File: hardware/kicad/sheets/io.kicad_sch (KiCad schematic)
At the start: 22 parts, among them J10 AUX, J11 INPUTS, Q2 AO3400A, U6 ULN2003A

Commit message: hardware: uncross the AUX bank - vent on GPIO16, U6 channels reversed
U6's outputs sit level with their inputs, so channel 1 (pins 1/16, the
bottom of the SOIC) fed J10.2 at the top of the terminal and all three
output traces crossed, two of them through B.Cu. AUX1 now uses channel 3
and AUX3 channel 1, so O3/O2/O1 fan straight across to J10.2/3/4 on F.Cu
with no via (was 1/1/0 vias).

The input copper was already in the order the board's geography forces:
U6's top input escapes by the B.Cu lane north to U1 pin 9, the bottom
one by the route south of LCD_CS to U1 pin 22. Rather than re-route it,
the GPIOs follow it: vent (AUX1) moves GPIO14 -> GPIO16, AUX3 moves
GPIO16 -> GPIO14, AUX2 stays on GPIO15. The existing input tracks keep
their geometry under the swapped names, and R23/R25 trade places so each
pulldown stays on the input it terminates. U6->J10 is wired by label
pairs now, since the schematic can't draw the swap without a crossing.

Kconfig defaults, pin-assignments, the roadmap, the KiCad README and
DESIGN-NOTES follow. An existing local sdkconfig keeps the old values
until KILN_PIN_VENT / KILN_PIN_AUX3 are reset.

Co-Authored-By: Claude Opus 5.5 <noreply@anthropic.com>
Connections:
- net AUX1: now also U6.3 (I3); no longer U6.1 (I1)
- net AUX1_OUT: now also U6.14 (O3); no longer U6.16 (O1)
- net AUX3: now also U6.1 (I1); no longer U6.3 (I3)
- net AUX3_OUT: now also U6.16 (O1); no longer U6.14 (O3)
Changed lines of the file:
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@@
-	(wire
-		(pts
-			(xy 50.8 48.26) (xy 73.66 48.26)
-		)
-		(stroke
-			(width 0)
-			(type default)
-		)
-	)
 	(wire
 		(pts
@@
 		(pts
 			(xy 370.84 43.18) (xy 370.84 40.64)
-		)
-		(stroke
-			(width 0)
-			(type default)
-		)
-	)
-	(wire
-		(pts
-			(xy 50.8 53.34) (xy 73.66 53.34)
 		)
 		(stroke
@@
 	)
 	(label "AUX3_OUT"
-		(at 62.23 53.34 180)
+		(at 73.66 53.34 180)
 		(effects
 			(font
@@
 	)
 	(label "AUX1_OUT"
-		(at 62.23 48.26 180)
+		(at 73.66 48.26 180)
 		(effects
 			(font
@@
 			)
 			(justify right bottom)
+		)
+	)
+	(label "AUX3_OUT"
+		(at 50.8 48.26 0)
+		(effects
+			(font
+				(size 1.27 1.27)
+			)
+			(justify left bottom)
 		)
 	)
@@
 		)
 	)
+	(label "AUX1_OUT"
+		(at 50.8 53.34 0)
+		(effects
+			(font
+				(size 1.27 1.27)
+			)
+			(justify left bottom)
+		)
+	)
 	(label "BUZZ_K"
 		(at 175.26 49.53 0)
@@
 		)
 	)
+	(global_label "AUX3"
+		(shape passive)
+		(at 27.94 48.26 180)
+		(effects
+			(font
+				(size 1.27 1.27)
+			)
+			(justify right)
+		)
+		(property "Intersheetrefs" "${INTERSHEET_REFS}"
+			(at 27.94 48.26 0)
+			(hide yes)
+			(show_name no)
+			(do_not_autoplace no)
+			(effects
+				(font
+					(size 1.27 1.27)
+				)
+			)
+		)
+	)
 	(global_label "AUX1"
 		(shape passive)
@@
 		)
 	)
+	(global_label "AUX1"
+		(shape passive)
+		(at 27.94 53.34 180)
+		(effects
+			(font
+				(size 1.27 1.27)
+			)
+			(justify right)
+		)
+		(property "Intersheetrefs" "${INTERSHEET_REFS}"
+			(at 27.94 53.34 0)
+			(hide yes)
+			(show_name no)
+			(do_not_autoplace no)
+			(effects
+				(font
+					(size 1.27 1.27)
+				)
+			)
+		)
+	)
 	(global_label "AUX2"
 		(shape passive)
@@
 		)
 	)
-	(global_label "AUX1"
-		(shape passive)
-		(at 27.94 48.26 180)
-		(effects
-			(font
-				(size 1.27 1.27)
-			)
-			(justify right)
-		)
-		(property "Intersheetrefs" "${INTERSHEET_REFS}"
-			(at 27.94 48.26 0)
-			(hide yes)
-			(show_name no)
-			(do_not_autoplace no)
-			(effects
-				(font
-					(size 1.27 1.27)
-				)
-			)
-		)
-	)
 	(global_label "IN2"
 		(shape passive)
@@
 			(hide yes)
 			(show_name no)
-			(do_not_autoplace no)
-			(effects
-				(font
-					(size 1.27 1.27)
-				)
-			)
-		)
-	)
-	(global_label "AUX3"
-		(shape passive)
-		(at 27.94 53.34 180)
-		(effects
-			(font
-				(size 1.27 1.27)
-			)
-			(justify right)
-		)
-		(property "Intersheetrefs" "${INTERSHEET_REFS}"
-			(at 27.94 53.34 0)
-			(hide yes)
-			(show_name no)

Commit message: hardware: TC1_CS and IN3 trade GPIOs, D5 channels follow the copper
TC1_CS kept rev A's TC_CS pad through the rename - U1 pin 18, on the
module's bottom edge - so it ran back up under U1 on B.Cu to reach U3 at
the top right, while IN3 left pin 39 at the top right and came all the
way down to its filter block at the bottom left. The two crossed and each
ran the long way round. They now trade pins: TC1_CS on pin 39 (GPIO1),
IN3 on pin 18 (GPIO10). IN3 stays on an ADC1-capable GPIO, so the
resistance-monitored interlock is still possible without a respin.
TC1_CS + IN3: 197 mm / 11 vias -> 167 mm / 5.

D5's four SRV05-4 channels are interchangeable, like U6's. IN3_RAW sat on
IO3 (pin 4), on the side facing J11, and crossed IN2_RAW through 3 vias
to reach R28 west of D5. IN2_RAW now uses the idle IO4 (pin 6), IN3_RAW
IO2 (pin 3), and IO3 is the idle one: IN3_RAW is 0 vias, all F.Cu.

Across the five nets (TC1_CS, IN3, IN1/2/3_RAW): 287 mm / 18 vias ->
260 mm / 7. Board copper changes only on those nets, five pads re-netted,
no part moved, silk unchanged.

Kconfig defaults (KILN_PIN_TC1_CS 10 -> 1, KILN_PIN_IN_SPARE 1 -> 10),
pin-assignments, DESIGN-NOTES and the firmware backlog follow; the
backlog's AUX row was also still on the pre-#368 numbers. An existing
local sdkconfig keeps the old values until those two are reset.

Co-Authored-By: Claude Opus 5.5 <noreply@anthropic.com>
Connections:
- net IN2_RAW: now also D5.6 (IO4); no longer D5.3 (IO2)
- net IN3_RAW: now also D5.3 (IO2); no longer D5.4 (IO3)
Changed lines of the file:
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@@
-	)
-	(junction
-		(at 281.94 64.77)
-		(diameter 0)
-		(color 0 0 0 0)
 	)
 	(junction
@@
 	)
 	(no_connect
-		(at 323.85 64.77)
-	)
-	(no_connect
 		(at 30.48 63.5)
 	)
@@
 	)
 	(no_connect
+		(at 323.85 59.69)
+	)
+	(no_connect
 		(at 30.48 58.42)
 	)
@@
 	(wire
 		(pts
-			(xy 323.85 59.69) (xy 326.39 59.69)
-		)
-		(stroke
-			(width 0)
-			(type default)
-		)
-	)
-	(wire
-		(pts
 			(xy 355.6 44.45) (xy 355.6 41.91)
 		)
@@
 	(wire
 		(pts
-			(xy 281.94 64.77) (xy 298.45 64.77)
-		)
-		(stroke
-			(width 0)
-			(type default)
-		)
-	)
-	(wire
-		(pts
 			(xy 160.02 49.53) (xy 157.48 49.53)
 		)
@@
 	(wire
 		(pts
+			(xy 298.45 64.77) (xy 295.91 64.77)
+		)
+		(stroke
+			(width 0)
+			(type default)
+		)
+	)
+	(wire
+		(pts
 			(xy 290.83 46.99) (xy 288.29 46.99)
 		)
@@
 		(pts
 			(xy 30.48 48.26) (xy 27.94 48.26)
+		)
+		(stroke
+			(width 0)
+			(type default)
+		)
+	)
+	(wire
+		(pts
+			(xy 323.85 64.77) (xy 326.39 64.77)
 		)
 		(stroke
@@
 	)
 	(label "IN2_RAW"
+		(at 326.39 64.77 0)
+		(effects
+			(font
+				(size 1.27 1.27)
+			)
+			(justify left bottom)
+		)
+	)
+	(label "IN2_RAW"
 		(at 281.94 44.45 0)
 		(effects
@@
 		)
 	)
+	(global_label "IN3_RAW"
+		(shape passive)
+		(at 295.91 64.77 180)
+		(effects
+			(font
+				(size 1.27 1.27)
+			)
+			(justify right)
+		)
+		(property "Intersheetrefs" "${INTERSHEET_REFS}"
+			(at 295.91 64.77 0)
+			(hide yes)
+			(show_name no)
+			(do_not_autoplace no)
+			(effects
+				(font
+					(size 1.27 1.27)
+				)
+			)
+		)
+	)
 	(global_label "AUX3"
 		(shape passive)
@@
 			(hide yes)
 			(show_name no)
-			(do_not_autoplace no)
-			(effects
-				(font
-					(size 1.27 1.27)
-				)
-			)
-		)
-	)
-	(global_label "IN3_RAW"
-		(shape passive)
-		(at 326.39 59.69 0)
-		(effects
-			(font
-				(size 1.27 1.27)
-			)
-			(justify left)
-		)
-		(property "Intersheetrefs" "${INTERSHEET_REFS}"
-			(at 326.39 59.69 0)
-			(hide yes)
-			(show_name no)

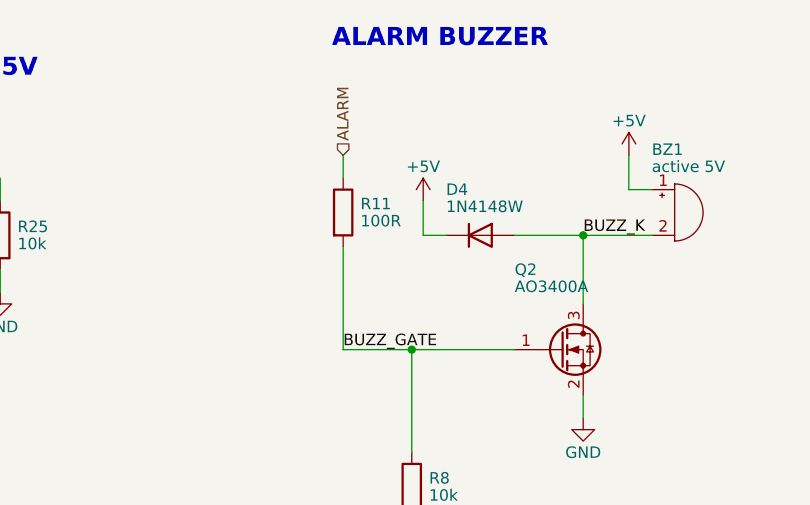
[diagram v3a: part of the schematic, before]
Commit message: hardware: flags at their sources, tri-state MAX31856, Q4 flipped, make erc
Second batch from SCHEMATIC-REVIEW-2026-10-22.md (findings 5, 7, 14, 15,
16 and the local half of 19).

PWR_FLAGs: the power sheet's parked corner is gone. Each flag now sits
where its rail is created - J2.1 (VIN), J2.2 (GND), Q8 source (VIN_P),
L1 output (BUCK_5V) and J1 pin A4 (VBUS, on the mcu sheet) - with the
value text shown on all of them.

MAX31856: U3 and U5 now use bisque:MAX31856 from the new project library
bisque.kicad_sym (registered in sym-lib-table), a copy of the KiCad
symbol with SDO typed tri-state, which is what the part does while CS is
high. The ERC exclusion that papered over the shared SPI_MISO is removed;
ERC is clean with no exclusions.

Q4 is mirrored so the high-side P-FET reads source-up to +5V and drain
down to SSR_EN. One Value string per LCSC part (C38/C44/C45 22uF/25V,
R11 100R 1%); C46 moved 5 mm right to clear the longer text. Every test
point's Value is its net name (TP1 "+3V3" ... TP12 "WDT_CT_P"), so the
board's Value fields, the JLC BOM and the schematic PDF regenerate.

make erc runs kicad-cli ERC at every severity and fails on any
violation; lib_symbol_mismatch, endpoint_off_grid and
same_local_global_label are promoted to errors in the project. It is not
part of pcb-check or CI on purpose.

Board: sync changed only Value fields (0 re-netted); gerbers differ by
timestamp only; DRC 0; full make pcb-check passes.

Co-Authored-By: Claude Fable 5.1 <noreply@anthropic.com>
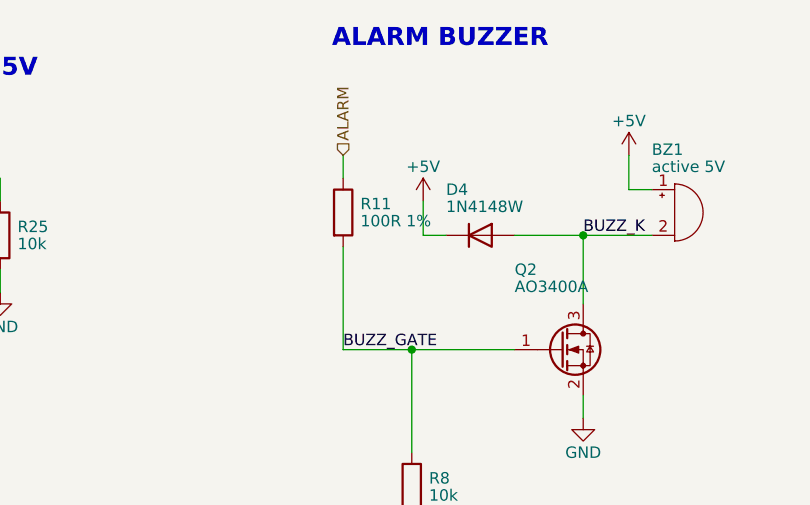
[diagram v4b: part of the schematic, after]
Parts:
- R11: value 100R -> 100R 1%
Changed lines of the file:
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@@
 			)
 		)
-		(property "Value" "100R"
+		(property "Value" "100R 1%"
 			(at 150.506 47.94 0)
 			(show_name no)

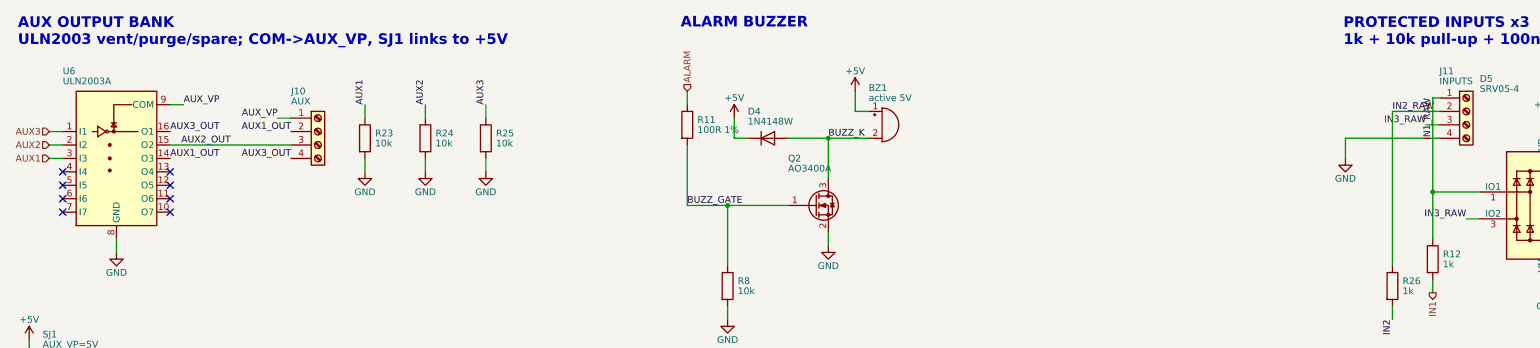
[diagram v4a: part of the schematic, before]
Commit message: hardware: honest symbols, real MPNs, U6 spares grounded, LCD_RST verified
Third batch from SCHEMATIC-REVIEW-2026-10-22.md (findings 6, 8, 11, 17,
18 and E1/E2).

Symbols: D8 is bisque:SMAJ30A (drawn as a zener with its cathode on the
rail, since the fitted TVS is unidirectional), Q5-Q7 are bisque:CJ2310
and U2 is bisque:TLV1117LV33, each a flattened copy of the stock symbol
with the fitted part's name, description and LCSC-hosted datasheet, so
no pin or wire moved. The stock D_TVS, 2N7002 and TLV1117-33 embeds are
gone from the sheets.

Sourcing: every one of the 160 assembled symbols now carries MPN (the
manufacturer's part number, from LCSC's product record for its C-number),
Manufacturer and Datasheet (LCSC's hosted PDF) beside LCSC. check_mpn.py
keeps LCSC tied to gen_jlc.LCSC and requires the other two to be present
and MPN not to be a bare C-number.

Drawing: J11's IN1_RAW/IN2_RAW labels read along their own wires instead
of across the connector; U6's unused Darlington inputs I4-I7 are tied to
GND (the board's F.Cu pour already covers them - 4 pads re-netted, 0
unconnected, DRC 0); the root notes record the retired designators and
the LCD_RST finding (the MSP4021's own schematic shows no pull-up on
RESET, so GPIO46 does not block download mode); the mcu sheet notes that
GPIO35/36 rule out R8 (octal PSRAM) modules.

The datasheet manifest maps the shared 22uF/25V sheet to the unified
value and exempts the test points' net-name values. Full make pcb-check
passes; gerbers differ by timestamp and the re-filled GND pour; 3D
renders refreshed.

Co-Authored-By: Claude Fable 5.1 <noreply@anthropic.com>
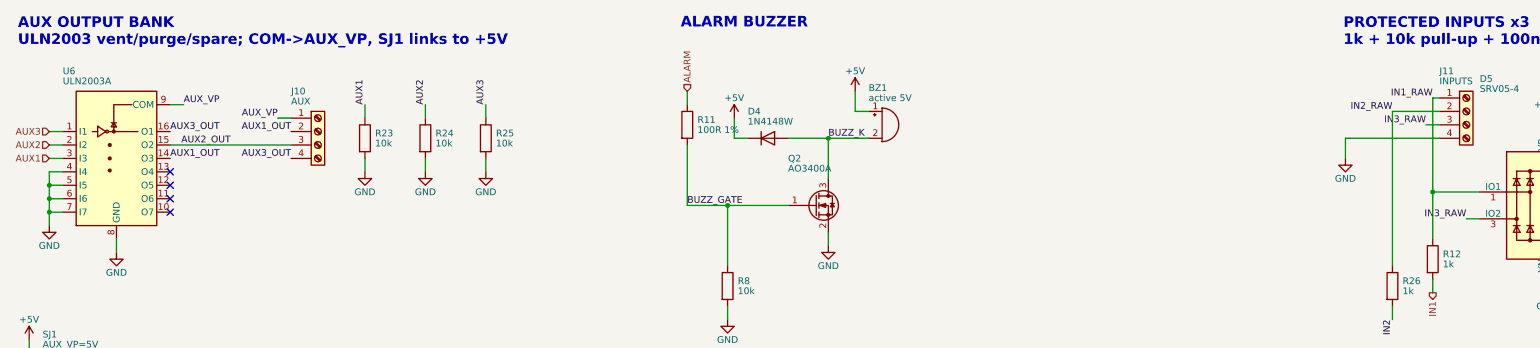
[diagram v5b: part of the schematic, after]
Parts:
- BZ1: MPN C96093 -> TMB12A05; Manufacturer (none) -> Huaneng
- C12, C23, C24: MPN C49678 -> CC0805KRX7R9BB104; Manufacturer (none) -> YAGEO
- D4: MPN C81598 -> 1N4148W; Manufacturer (none) -> ST(Semtech)
- D5: MPN C7420376 -> SRV05-4; Manufacturer (none) -> R+O
- J10, J11: MPN C42377749 -> WJ500V-5.08-04P-14-00A; Manufacturer (none) -> KANGNEX
- Q2: MPN C20917 -> AO3400A; Manufacturer (none) -> AOS
- R11: MPN C17408 -> 0805W8F1000T5E; Manufacturer (none) -> UNI-ROYAL
- R12, R26, R28: MPN C17513 -> 0805W8F1001T5E; Manufacturer (none) -> UNI-ROYAL
- R13, R23, R24, R25, R27, R29, R8: MPN C17414 -> 0805W8F1002T5E; Manufacturer (none) -> UNI-ROYAL
- U6: MPN C7512 -> ULN2003ADR; Manufacturer (none) -> TI
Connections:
- net GND: now also U6.4 (I4), U6.5 (I5), U6.6 (I6), U6.7 (I7)
- no-connect marks 9 -> 5
